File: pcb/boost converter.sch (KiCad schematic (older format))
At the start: 13 parts, among them Q1 IRF740, U5 MAX1771

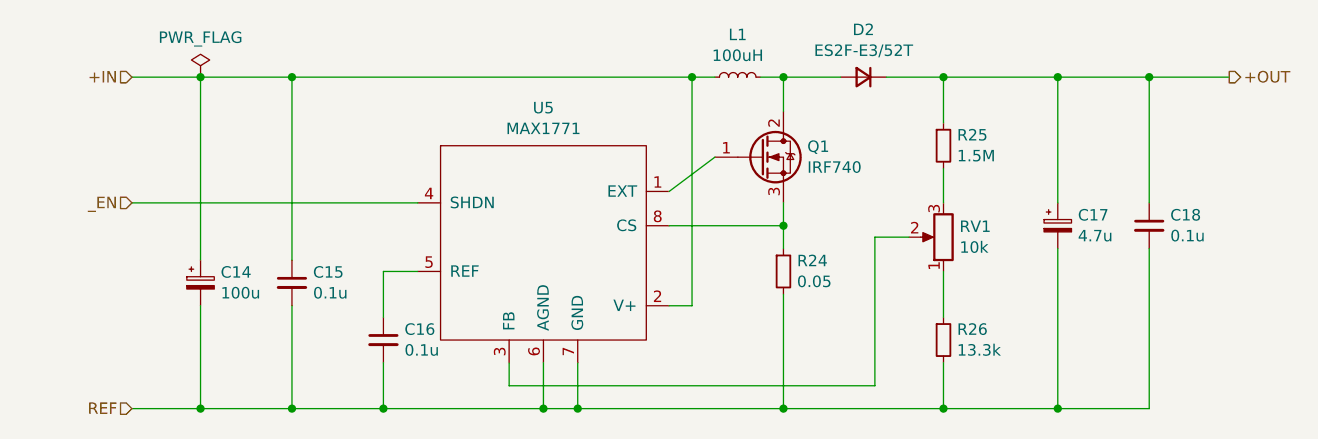
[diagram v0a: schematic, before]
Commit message: Update PCB and schematic files with mostly small tweaks. Added DRC rules added to .pro, and changes on layout and footprints to reflect that.
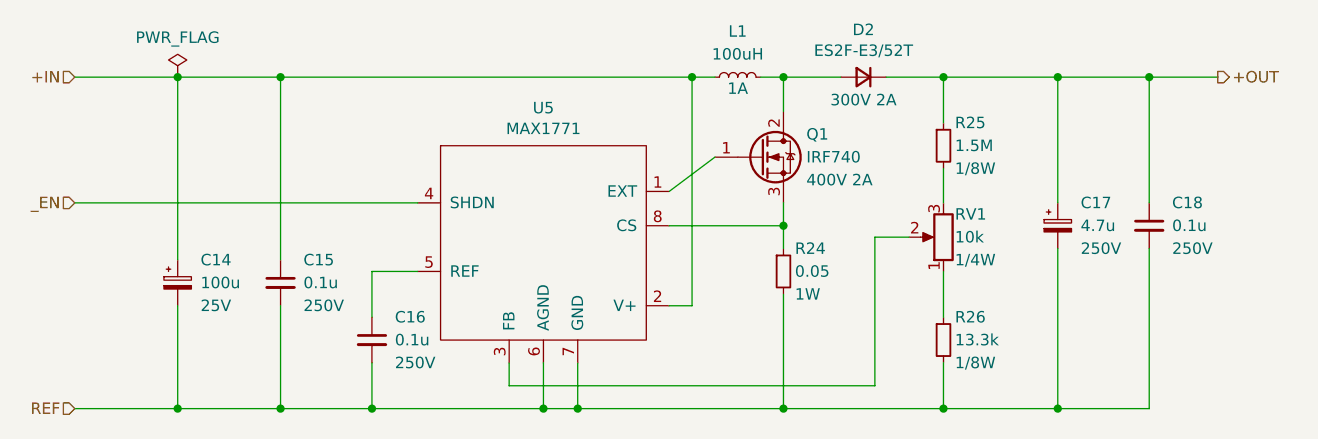
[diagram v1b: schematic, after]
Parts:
- C14: footprint Capacitors_SMD:CP_Elec_5x5.3 -> Capacitors_SMD:CP_Elec_6.3x7.7; Digikey Page https://www.digikey.com/en/products/detail/nichicon/UWR1A10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 -> https://www.digikey.com/en/products/detail/rubycon/25TZV100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; Rating (none) -> 25V
- C15, C16, C17: Rating (none) -> 250V
- C18: footprint Capacitors_SMD:C_0805_HandSoldering -> Capacitors_SMD:C_1206_HandSoldering; Digikey Page https://www.digikey.com/en/products/detail/tdk-corporation/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 -> https://www.digikey.com/en/products/detail/yageo/CC1206KKX7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; Rating (none) -> 250V
- D2: Rating (none) -> 300V 2A
- L1: Rating (none) -> 1A
- Q1: Rating (none) -> 400V 2A
- R24: Digikey Page https://www.digikey.com/en/products/detail/delta-electronic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 -> https://www.digikey.com/en/products/detail/panasonic-electr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; Rating (none) -> 1W
- R25, R26: Rating (none) -> 1/8W
- RV1: Rating (none) -> 1/4W
- U5: footprint SMD_Packages:SOIC-8-N -> Housings_SOIC:SOIC-8_3.9x4.9mm_Pitch1.27mm; Rating (none) -> 16.5V
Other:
- moved on the sheet: C14, C15, C16

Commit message: Add alternate parts for BOM, adjust micro to be more compatible with new PIC24FJ series parts.
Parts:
- C14: Alt Datasheet (none) -> https://media.digikey.com/pdf/Data%20Sheets/NextGen%20Compo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; Alt Digikey (none) -> https://www.digikey.com/en/products/detail/aillen/UT107M025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
- C15, C16, C17, C18, D2, L1, R24, R25, R26, RV1, U5: Alt Datasheet (none) -> -; Alt Digikey (none) -> -
- Q1: Alt Datasheet (none) -> https://www.st.com/content/ccc/resource/technical/document/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; Alt Digikey (none) -> https://www.digikey.com/en/products/detail/stmicroelectroni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
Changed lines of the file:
@@
 F 4 "https://www.digikey.com/en/products/detail/analog-devices-inc-maxim-integrated/MAX1771CSA-T/1520601" H 5550 3600 50  0001 C CNN "Digikey Page"
 F 5 "16.5V" H 5550 3600 50  0001 C CNN "Rating"
+F 6 "-" H 5550 3600 50  0001 C CNN "Alt Datasheet"
+F 7 "-" H 5550 3600 50  0001 C CNN "Alt Digikey"
 	1    5550 3600
 	1    0    0    -1
@@
 F 4 "https://www.digikey.com/en/products/detail/taiyo-yuden/NR8040T101M/1739086" H 6400 2950 50  0001 C CNN "Digikey Page"
 F 5 "1A" V 6350 2950 50  0000 C CNN "Rating"
+F 6 "-" H 6400 2950 50  0001 C CNN "Alt Datasheet"
+F 7 "-" H 6400 2950 50  0001 C CNN "Alt Digikey"
 	1    6400 2950
 	0    -1   -1   0
@@
 F 4 "https://www.digikey.com/en/products/detail/vishay-general-semiconductor-diodes-division/ES2F-E3-52T/1091445" H 6950 2950 50  0001 C CNN "Digikey Page"
 F 5 "300V 2A" H 6950 3050 50  0000 C CNN "Rating"
+F 6 "-" H 6950 2950 50  0001 C CNN "Alt Datasheet"
+F 7 "-" H 6950 2950 50  0001 C CNN "Alt Digikey"
 	1    6950 2950
 	-1   0    0    1
@@
 F 4 "https://www.digikey.com/en/products/detail/tdk-corporation/CGA4J3X7T2E104K125AA/2672869" H 4800 4100 50  0001 C CNN "Digikey Page"
 F 5 "250V" H 4900 4000 50  0000 L CNN "Rating"
+F 6 "-" H 4800 4100 50  0001 C CNN "Alt Datasheet"
+F 7 "-" H 4800 4100 50  0001 C CNN "Alt Digikey"
 	1    4800 4100
 	1    0    0    -1
@@
 F 4 "https://www.digikey.com/en/products/detail/panasonic-electronic-components/ERJ-8CWJR050V/4927034" H 6600 3800 50  0001 C CNN "Digikey Page"
 F 5 "1W" H 6650 3700 50  0000 L CNN "Rating"
+F 6 "-" H 6600 3800 50  0001 C CNN "Alt Datasheet"
+F 7 "-" H 6600 3800 50  0001 C CNN "Alt Digikey"
 	1    6600 3800
 	1    0    0    -1
@@
 F 4 "https://www.digikey.com/en/products/detail/yageo/RC0805FR-101M5L/14286567" H 7300 3250 50  0001 C CNN "Digikey Page"
 F 5 "1/8W" H 7350 3150 50  0000 L CNN "Rating"
+F 6 "-" H 7300 3250 50  0001 C CNN "Alt Datasheet"
+F 7 "-" H 7300 3250 50  0001 C CNN "Alt Digikey"
 	1    7300 3250
 	1    0    0    -1
@@
 F 4 "https://www.digikey.com/en/products/detail/yageo/RC0805FR-0713K3L/727586" H 7300 4100 50  0001 C CNN "Digikey Page"
 F 5 "1/8W" H 7350 4000 50  0000 L CNN "Rating"
+F 6 "-" H 7300 4100 50  0001 C CNN "Alt Datasheet"
+F 7 "-" H 7300 4100 50  0001 C CNN "Alt Digikey"
 	1    7300 4100
 	1    0    0    -1
@@
 F 4 "https://www.digikey.com/en/products/detail/yageo/CC1206KKX7RYBB104/5195382" H 8200 3600 50  0001 C CNN "Digikey Page"
 F 5 "250V" H 8300 3500 50  0000 L CNN "Rating"
+F 6 "-" H 8200 3600 50  0001 C CNN "Alt Datasheet"
+F 7 "-" H 8200 3600 50  0001 C CNN "Alt Digikey"
 	1    8200 3600
 	1    0    0    -1
@@
 F 4 "https://www.digikey.com/en/products/detail/nichicon/UPS2E4R7MPD1TD/3129739" H 7800 3600 50  0001 C CNN "Digikey Page"
 F 5 "250V" H 7900 3500 50  0000 L CNN "Rating"
+F 6 "-" H 7800 3600 50  0001 C CNN "Alt Datasheet"
+F 7 "-" H 7800 3600 50  0001 C CNN "Alt Digikey"
 	1    7800 3600
 	1    0    0    -1
@@
 F 4 "https://www.digikey.com/en/products/detail/bourns-inc/3214X-1-103E/1817397" H 7300 3650 50  0001 C CNN "Digikey Page"
 F 5 "1/4W" H 7250 3750 50  0000 R CNN "Rating"
+F 6 "-" H 7300 3650 50  0001 C CNN "Alt Datasheet"
+F 7 "-" H 7300 3650 50  0001 C CNN "Alt Digikey"
 	1    7300 3650
 	-1   0    0    1
@@
 F 4 "https://www.digikey.com/en/products/detail/vishay-siliconix/IRF740ASPBF/812108" H 6500 3300 50  0001 C CNN "Digikey Page"
 F 5 "400V 2A" H 6700 3200 50  0000 L CNN "Rating"
+F 6 "https://www.st.com/content/ccc/resource/technical/document/datasheet/44/4c/24/37/1f/95/4d/c1/CD00003028.pdf/files/CD00003028.pdf/jcr:content/translations/en.CD00003028.pdf" H 6500 3300 50  0001 C CNN "Alt Datasheet"
+F 7 "https://www.digikey.com/en/products/detail/stmicroelectronics/STB11NK40ZT4/2022881" H 6500 3300 50  0001 C CNN "Alt Digikey"
 	1    6500 3300
 	1    0    0    -1
@@
 F 4 "https://www.digikey.com/en/products/detail/rubycon/25TZV100M6-3X8/3134865" H 3950 3850 50  0001 C CNN "Digikey Page"
 F 5 "25V" H 4050 3750 50  0000 L CNN "Rating"
+F 6 "https://media.digikey.com/pdf/Data%20Sheets/NextGen%20Components%20PDFs/UT107M025HEJTA.pdf" H 3950 3850 50  0001 C CNN "Alt Datasheet"
+F 7 "https://www.digikey.com/en/products/detail/aillen/UT107M025HEJTA/15282268" H 3950 3850 50  0001 C CNN "Alt Digikey"
 	1    3950 3850
 	1    0    0    -1
@@
 F 4 "https://www.digikey.com/en/products/detail/tdk-corporation/CGA4J3X7T2E104K125AA/2672869" H 4400 3850 50  0001 C CNN "Digikey Page"
 F 5 "250V" H 4500 3750 50  0000 L CNN "Rating"
+F 6 "-" H 4400 3850 50  0001 C CNN "Alt Datasheet"
+F 7 "-" H 4400 3850 50  0001 C CNN "Alt Digikey"
 	1    4400 3850
 	1    0    0    -1

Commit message: Update schematic with some better part selection, reducing BOM. Update PCB for panelized fabrication.
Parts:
- C14: footprint Capacitors_SMD:CP_Elec_6.3x7.7 -> Capacitors_SMD:CP_Elec_6.3x5.8; Alt Datasheet https://media.digikey.com/pdf/Data%20Sheets/NextGen%20Compo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 -> https://www.nichicon.co.jp/english/products/pdfs/e-uzs.pdf; Alt Digikey https://www.digikey.com/en/products/detail/aillen/UT107M025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 -> https://www.digikey.com/en/products/detail/nichicon/UZS0J10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
- R25: value 1.5M -> 1M; Digikey Page https://www.digikey.com/en/products/detail/yageo/RC0805FR-1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 -> https://www.digikey.com/en/products/detail/yageo/RC0805FR-0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
- R26: value 13.3k -> 2.2k; Digikey Page https://www.digikey.com/en/products/detail/yageo/RC0805FR-0713K3L/727586 -> https://www.digikey.com/en/products/detail/yageo/RC0805FR-072K2L/727676
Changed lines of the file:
@@
 P 7300 3250
 F 0 "R25" H 7350 3350 50  0000 L CNN
-F 1 "1.5M" H 7350 3250 50  0000 L CNN
+F 1 "1M" H 7350 3250 50  0000 L CNN
 F 2 "Resistors_SMD:R_0805_HandSoldering" H 7300 3250 50  0001 C CNN
 F 3 "https://www.yageo.com/upload/media/product/productsearch/datasheet/rchip/PYu-RC_Group_51_RoHS_L_11.pdf" H 7300 3250 50  0001 C CNN
-F 4 "https://www.digikey.com/en/products/detail/yageo/RC0805FR-101M5L/14286567" H 7300 3250 50  0001 C CNN "Digikey Page"
+F 4 "https://www.digikey.com/en/products/detail/yageo/RC0805FR-071ML/727445" H 7300 3250 50  0001 C CNN "Digikey Page"
 F 5 "1/8W" H 7350 3150 50  0000 L CNN "Rating"
 F 6 "-" H 7300 3250 50  0001 C CNN "Alt Datasheet"
@@
 P 7300 4100
 F 0 "R26" H 7350 4200 50  0000 L CNN
-F 1 "13.3k" H 7350 4100 50  0000 L CNN
+F 1 "2.2k" H 7350 4100 50  0000 L CNN
 F 2 "Resistors_SMD:R_0805_HandSoldering" H 7300 4100 50  0001 C CNN
 F 3 "https://www.yageo.com/upload/media/product/productsearch/datasheet/rchip/PYu-RC_Group_51_RoHS_L_11.pdf" H 7300 4100 50  0001 C CNN
-F 4 "https://www.digikey.com/en/products/detail/yageo/RC0805FR-0713K3L/727586" H 7300 4100 50  0001 C CNN "Digikey Page"
+F 4 "https://www.digikey.com/en/products/detail/yageo/RC0805FR-072K2L/727676" H 7300 4100 50  0001 C CNN "Digikey Page"
 F 5 "1/8W" H 7350 4000 50  0000 L CNN "Rating"
 F 6 "-" H 7300 4100 50  0001 C CNN "Alt Datasheet"
@@
 F 0 "C14" H 4050 3950 50  0000 L CNN
 F 1 "100u" H 4050 3850 50  0000 L CNN
-F 2 "Capacitors_SMD:CP_Elec_6.3x7.7" H 3950 3850 50  0001 C CNN
+F 2 "Capacitors_SMD:CP_Elec_6.3x5.8" H 3950 3850 50  0001 C CNN
 F 3 "https://www.rubycon.co.jp/wp-content/uploads/catalog-aluminum/TZV.pdf" H 3950 3850 50  0001 C CNN
 F 4 "https://www.digikey.com/en/products/detail/rubycon/25TZV100M6-3X8/3134865" H 3950 3850 50  0001 C CNN "Digikey Page"
 F 5 "25V" H 4050 3750 50  0000 L CNN "Rating"
-F 6 "https://media.digikey.com/pdf/Data%20Sheets/NextGen%20Components%20PDFs/UT107M025HEJTA.pdf" H 3950 3850 50  0001 C CNN "Alt Datasheet"
-F 7 "https://www.digikey.com/en/products/detail/aillen/UT107M025HEJTA/15282268" H 3950 3850 50  0001 C CNN "Alt Digikey"
+F 6 "https://www.nichicon.co.jp/english/products/pdfs/e-uzs.pdf" H 3950 3850 50  0001 C CNN "Alt Datasheet"
+F 7 "https://www.digikey.com/en/products/detail/nichicon/UZS0J101MCL1GB/2551047" H 3950 3850 50  0001 C CNN "Alt Digikey"
 	1    3950 3850
 	1    0    0    -1
